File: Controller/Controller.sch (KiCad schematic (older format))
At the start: 33 parts

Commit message: Controller schematic...
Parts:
- removed J?: USB_B_Mini, symbol Connector:USB_B_Mini
- removed U?: ATmega328P-AU, Package_QFP:TQFP-32_7x7mm_P0.8mm, symbol MCU_Microchip_ATmega:ATmega328P-AU
- added C1, C2: 330uF, symbol Device:CP_Small
- added C10, C12: 100nF, Capacitor_SMD:C_0805_2012Metric, symbol Device:C_Small
- added C11: 4u7, symbol Device:CP_Small
- added C21, C22, C24: 100n, Capacitor_SMD:C_0805_2012Metric, symbol Device:C_Small
- added C3, C6: 10nF, Capacitor_SMD:C_0805_2012Metric, symbol Device:C_Small
- added C4, C5: 100uF, symbol Device:CP_Small
- added C9: 10uF, Capacitor_SMD:C_0805_2012Metric, symbol Device:C_Small
- added D1, D2: BLUE, LED_SMD:LED_0805_2012Metric, symbol Device:LED
- added D3: SS1P3L, Diode_SMD:D_SOD-123, symbol Device:D
- added D4: ORANGE, LED_SMD:LED_0805_2012Metric, symbol Device:LED
- added D5: GREEN, LED_SMD:LED_0805_2012Metric, symbol Device:LED
- added D8: RED, LED_SMD:LED_0805_2012Metric, symbol Device:LED
- added F1: 4A, symbol Device:Fuse
- added F2: 1A, symbol Device:Fuse
- added F3: 500mA, Fuse:Fuse_1812_4532Metric, symbol Device:Polyfuse
- added J2: CON_15V, Connector_JST:JST_XH_B2B-XH-A_1x02_P2.50mm_Vertical, symbol Connector_Generic:Conn_01x02
- added J5: CON_5V, Connector_JST:JST_XH_B2B-XH-A_1x02_P2.50mm_Vertical, symbol Connector_Generic:Conn_01x02
- added J6: CON_5V_AUX, Connector_JST:JST_XH_B2B-XH-A_1x02_P2.50mm_Vertical, symbol Connector_Generic:Conn_01x02
- added J7: CON_USB_A, Connector_USB:USB_B_TE_5787834_Vertical, symbol Connector:USB_A
- added L1, L2, L3: 10uH, symbol Device:L_Small
- added Q1, Q2: SI4435FDY, Package_SO:SO-8_5.3x6.2mm_P1.27mm, symbol ak:Q_PMOS_SSSGDDDD
- added Q3: SQ2309ES, Package_TO_SOT_SMD:SOT-23, symbol Device:Q_PMOS_GSD
- added R1, R2, R3, R4, R7: 1k, Resistor_SMD:R_0805_2012Metric, symbol Device:R_Small
- added R11, R12: 10k, Resistor_SMD:R_0805_2012Metric, symbol Device:R_Small
- added R13: 330R, Resistor_SMD:R_0805_2012Metric, symbol Device:R_Small
- added SW1: SW_Push, Button_Switch_THT:SW_PUSH_6mm, symbol Switch:SW_Push
- added TP1, TP10, TP11, TP12, TP13, TP14, TP15, TP16, TP17, TP2, TP3, TP4, TP5, TP6, TP7, TP8, TP9: TestPoint_Alt, symbol Connector:TestPoint_Alt
- added U2: ATmega328P-AU, Package_QFP:TQFP-32_7x7mm_P0.8mm, symbol ak:ATmega328P-AU
- added U4: 74AHC1G14, Package_TO_SOT_SMD:SOT-23-5, symbol ak:74AHC1G14
- added U5: MCP6001-OT, Package_TO_SOT_SMD:SOT-23-5, symbol Amplifier_Operational:MCP6001-OT
- C13, C15, C16, C18, C20, C7, C8: renamed from C?; footprint (none) -> Capacitor_SMD:C_0805_2012Metric
- C14, C17, C19: renamed from C?; value 1uF -> 10nF; footprint (none) -> Capacitor_SMD:C_0805_2012Metric
- C23: renamed from C?; value 100nF -> 10nF; footprint (none) -> Capacitor_SMD:C_0805_2012Metric
- D6: renamed from D?; value RX RED -> RX ORANGE; footprint (none) -> LED_SMD:LED_0805_2012Metric
- D7: renamed from D?; footprint (none) -> LED_SMD:LED_0805_2012Metric
- F4: renamed from F?; footprint (none) -> Fuse:Fuse_1812_4532Metric
- J1: renamed from J?; value Signal out -> CON_TLC
- J3: renamed from J?; value ICSP -> CON_ICSP; footprint (none) -> Connector_IDC:IDC-Header_2x03_P2.54mm_Vertical
- R5, R6, R8, R9: renamed from R?; footprint (none) -> Resistor_SMD:R_0805_2012Metric
- Y1: renamed from Y?; value Resonator_Small -> 16MHz
- gave numbers to parts that had none: 10
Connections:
- net labels added: +15V, +3V3, +5VD, +BATT, FTDI_RX, FTDI_TX, LDR, LED, RTC_1PPS, RTC_32K, RTC_SCL, RTC_SDA, TLC_BLANK, TLC_LAT, TLC_SCL, TLC_SDA, USBD+, USBD-, ~RESET~, ~RTC_RST~
- net labels removed: BLANK, LAT, SCLK, SDAT, VCC, Vdrive
- wire segments 152 -> 306
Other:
- note added: "AUX POWER"
- note added: "DC SUPPLY"
- note added: "ICSP CONNECTOR"
- note added: "KICAD POWER FLAGS"
- note added: "LED DRIVER SIGNAL CONNECTOR"
- note added: "LIGHT SENSOR"
- note added: "MICROCONTROLLER"
- note added: "MOUNTING HOLES"
- note added: "REAL TIME CLOCK"
- note added: "RESET BUTTON"
- note added: "TEST POINTS"
- note added: "USB <-> SERIAL CONVERTER"
- note added: "USB POWER"
- moved on the sheet: C13, C14, C15, C16, C17, C18, C19, C20, C23, C7, C8, D6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

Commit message: Controller...
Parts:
- removed BT1: Battery_Cell, symbol Device:Battery_Cell
- removed C9: 10uF, Capacitor_SMD:C_0805_2012Metric, symbol Device:C_Small
- removed H3, H4: MountingHole_Pad, MountingHole:MountingHole_3.2mm_M3_Pad_Via, symbol Mechanical:MountingHole_Pad
- removed RV1: 100k, symbol Device:R_POT_TRIM
- added C25: 100n, Capacitor_SMD:C_0805_2012Metric, symbol Device:C_Small
- added C26: 1F, ak:FC0H105ZFTBR44, symbol Device:CP
- added C9: 4u7, Capacitor_SMD:C_Elec_4x5.8, symbol Device:CP_Small
- added D9: BAS716, Diode_SMD:D_SOD-523, symbol Device:D_Small
- added R14: 100R, Resistor_SMD:R_0805_2012Metric, symbol Device:R_Small
- added U6: MCP4012-xxxxCH, Package_TO_SOT_SMD:SOT-23-6, symbol Potentiometer_Digital:MCP4012-xxxxCH
- C1, C2: footprint (none) -> Capacitor_SMD:CP_Elec_10x10
- C11: footprint (none) -> Capacitor_SMD:C_Elec_4x5.8
- C4, C5: footprint (none) -> Capacitor_SMD:C_Elec_6.3x5.8
- F1, F2: footprint (none) -> ak:Fuseholder_SMD_Littelfuse_154
- J4: footprint ak:HARWIN_M20-7910842R -> ak:HARWIN_M20-8890845
- L1, L2, L3: footprint (none) -> Inductor_SMD:L_0805_2012Metric
- Q1, Q2: symbol ak:Q_PMOS_SSSGDDDD -> Controller-rescue:Q_PMOS_SSSGDDDD-ak
- TP1, TP10, TP11, TP12, TP13, TP14, TP15, TP16, TP17, TP2, TP3, TP4, TP5, TP6, TP7, TP8, TP9: footprint (none) -> TestPoint:TestPoint_Loop_D2.60mm_Drill1.6mm_Beaded
- U2: symbol ak:ATmega328P-AU -> Controller-rescue:ATmega328P-AU-ak
- Y1: footprint (none) -> ak:CSTNE
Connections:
- net labels added: POT_U~D~, ~POT_CS~
- wire segments 306 -> 321
- no-connect marks 0 -> 17
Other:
- moved on the sheet: C10, C19, C20, C21, C22, C23, C24, D4, F3, H1, H2, J6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

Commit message: Ground vias digit+colon. Placement/routing controller
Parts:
- C14, C15, C16, C17, C18, C19, C20: footprint Capacitor_SMD:C_0805_2012Metric -> Capacitor_SMD:C_0603_1608Metric
- J7: footprint Connector_USB:USB_B_TE_5787834_Vertical -> ak:UJ2-BV-1-TH
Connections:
- wire segments 321 -> 324
- no-connect marks 17 -> 16
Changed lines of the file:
@@
 EESchema Schematic File Version 4
 LIBS:Controller-cache
-EELAYER 29 0
+EELAYER 30 0
 EELAYER END
 $Descr A3 16535 11693
@@
 F 0 "C20" V 3500 6100 50  0000 C CNN
 F 1 "100nF" V 3500 5850 50  0000 C CNN
-F 2 "Capacitor_SMD:C_0805_2012Metric" H 3450 6000 50  0001 C CNN
+F 2 "Capacitor_SMD:C_0603_1608Metric" H 3450 6000 50  0001 C CNN
 F 3 "~" H 3450 6000 50  0001 C CNN
 	1    3450 6000
@@
 F 0 "C19" V 3500 5900 50  0000 C CNN
 F 1 "10nF" V 3500 5650 50  0000 C CNN
-F 2 "Capacitor_SMD:C_0805_2012Metric" H 3450 5800 50  0001 C CNN
+F 2 "Capacitor_SMD:C_0603_1608Metric" H 3450 5800 50  0001 C CNN
 F 3 "~" H 3450 5800 50  0001 C CNN
 	1    3450 5800
@@
 U 1 1 5D9BB567
 P 12850 4850
-F 0 "C18" H 12950 4800 50  0000 R CNN
+F 0 "C18" H 13050 4750 50  0000 R CNN
 F 1 "100nF" H 13100 4950 50  0000 R CNN
-F 2 "Capacitor_SMD:C_0805_2012Metric" H 12850 4850 50  0001 C CNN
+F 2 "Capacitor_SMD:C_0603_1608Metric" H 12850 4850 50  0001 C CNN
 F 3 "~" H 12850 4850 50  0001 C CNN
 	1    12850 4850
@@
 F 0 "C15" V 13200 4650 50  0000 R CNN
 F 1 "100nF" V 13200 5000 50  0000 R CNN
-F 2 "Capacitor_SMD:C_0805_2012Metric" H 13250 4700 50  0001 C CNN
+F 2 "Capacitor_SMD:C_0603_1608Metric" H 13250 4700 50  0001 C CNN
 F 3 "~" H 13250 4700 50  0001 C CNN
 	1    13250 4700
@@
 F 0 "C14" V 13000 4650 50  0000 R CNN
 F 1 "10nF" V 13000 4950 50  0000 R CNN
-F 2 "Capacitor_SMD:C_0805_2012Metric" H 13050 4700 50  0001 C CNN
+F 2 "Capacitor_SMD:C_0603_1608Metric" H 13050 4700 50  0001 C CNN
 F 3 "~" H 13050 4700 50  0001 C CNN
 	1    13050 4700
@@
 F 0 "C17" V 14100 4650 50  0000 R CNN
 F 1 "10nF" V 14100 4950 50  0000 R CNN
-F 2 "Capacitor_SMD:C_0805_2012Metric" H 14050 4700 50  0001 C CNN
+F 2 "Capacitor_SMD:C_0603_1608Metric" H 14050 4700 50  0001 C CNN
 F 3 "~" H 14050 4700 50  0001 C CNN
 	1    14050 4700
@@
 F 0 "C16" V 13900 4650 50  0000 R CNN
 F 1 "100nF" V 13900 5000 50  0000 R CNN
-F 2 "Capacitor_SMD:C_0805_2012Metric" H 13850 4700 50  0001 C CNN
+F 2 "Capacitor_SMD:C_0603_1608Metric" H 13850 4700 50  0001 C CNN
 F 3 "~" H 13850 4700 50  0001 C CNN
 	1    13850 4700
@@
 Text Label 10800 5400 0    50   ~ 10
 TLC_SCL
-Text Label 10800 5000 0    50   ~ 0
+Text Label 10800 5200 0    50   ~ 0
 TLC_LAT
 Text Label 10800 5100 0    50   ~ 0
@@
 F 0 "J7" H 5900 5150 50  0000 C CNN
 F 1 "CON_USB_A" H 6300 4450 50  0000 C CNN
-F 2 "Connector_USB:USB_B_TE_5787834_Vertical" H 6200 4750 50  0001 C CNN
+F 2 "ak:UJ2-BV-1-TH" H 6200 4750 50  0001 C CNN
 F 3 " ~" H 6200 4750 50  0001 C CNN
 	1    6050 4800
@@
 Wire Wire Line
 	2450 2550 2800 2550
-Wire Wire Line
-	11250 4200 10800 4200
-Text Label 10950 4200 2    50   ~ 0
-LED
 Wire Notes Line
 	11750 1150 13000 1150
@@
 	10800 4400 11250 4400
 NoConn ~ 12600 5100
-NoConn ~ 12600 5200
-NoConn ~ 11250 5200
 NoConn ~ 11250 6300
 NoConn ~ 11250 6400
@@
 	-1   0    0    1
 $EndComp
+Wire Wire Line
+	11250 5200 10800 5200
+Wire Wire Line
+	12600 5200 12650 5200
+Wire Wire Line
+	12650 5200 12650 5400
+Wire Wire Line
+	12650 5400 13650 5400
+NoConn ~ 11250 4200
 $EndSCHEMATC

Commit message: Routing controller
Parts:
- removed D9: BAS716, Diode_SMD:D_SOD-523, symbol Device:D_Small
- added D9: SS1P3L, Diode_SMD:D_SOD-123, symbol Device:D
- added R15: 47k, Resistor_SMD:R_0603_1608Metric, symbol Device:R_Small
- C10, C12, C13, C21, C22, C23, C24, C25, C6, C7, C8: footprint Capacitor_SMD:C_0805_2012Metric -> Capacitor_SMD:C_0603_1608Metric
- D1, D2, D4, D5, D6, D7, D8: footprint LED_SMD:LED_0805_2012Metric -> LED_SMD:LED_0603_1608Metric
- R1, R11, R12, R13, R14, R2, R3, R4, R5, R6, R7, R8, R9: footprint Resistor_SMD:R_0805_2012Metric -> Resistor_SMD:R_0603_1608Metric
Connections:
- net labels removed: +3V3
- wire segments 324 -> 323
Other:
- moved on the sheet: C23, R14

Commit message: layout...
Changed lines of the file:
@@
 EESchema Schematic File Version 4
 LIBS:Controller-cache
-EELAYER 29 0
+EELAYER 30 0
 EELAYER END
 $Descr A3 16535 11693
@@
 Wire Notes Line
 	950  9350 950  7500
+Text Label 10800 4300 0    50   ~ 0
+POT_U~D~
 Text Label 10800 4400 0    50   ~ 0
-POT_U~D~
-Text Label 10800 4300 0    50   ~ 0
 ~POT_CS~
 Wire Wire Line
@@
 	2750 8700 2750 8550
 $Comp
-L power:+5V #PWR?
+L power:+5V #PWR0104
 U 1 1 5DC2D6B5
 P 5850 7850
-F 0 "#PWR?" H 5850 7700 50  0001 C CNN
+F 0 "#PWR0104" H 5850 7700 50  0001 C CNN
 F 1 "+5V" H 5865 8023 50  0000 C CNN
 F 2 "" H 5850 7850 50  0001 C CNN
@@
 $EndComp
 $Comp
-L power:+5V #PWR?
+L power:+5V #PWR0105
 U 1 1 5DC2D918
 P 6900 7850
-F 0 "#PWR?" H 6900 7700 50  0001 C CNN
+F 0 "#PWR0105" H 6900 7700 50  0001 C CNN
 F 1 "+5V" H 6915 8023 50  0000 C CNN
 F 2 "" H 6900 7850 50  0001 C CNN

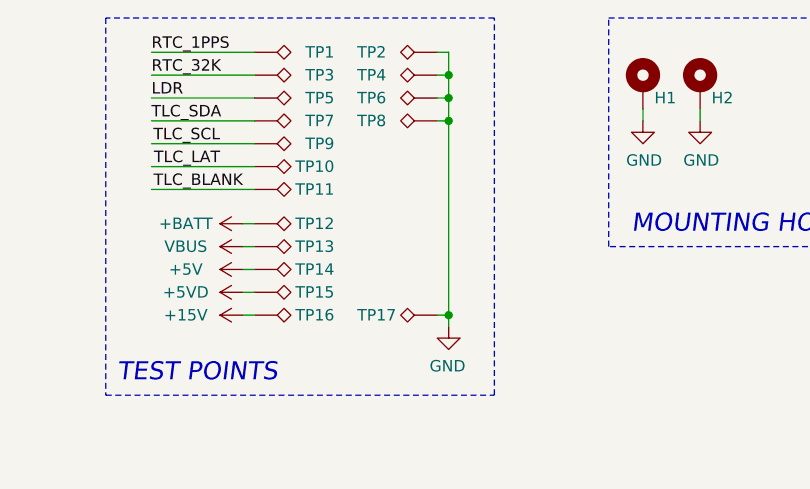
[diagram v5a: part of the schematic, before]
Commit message: Created mounting bracket.
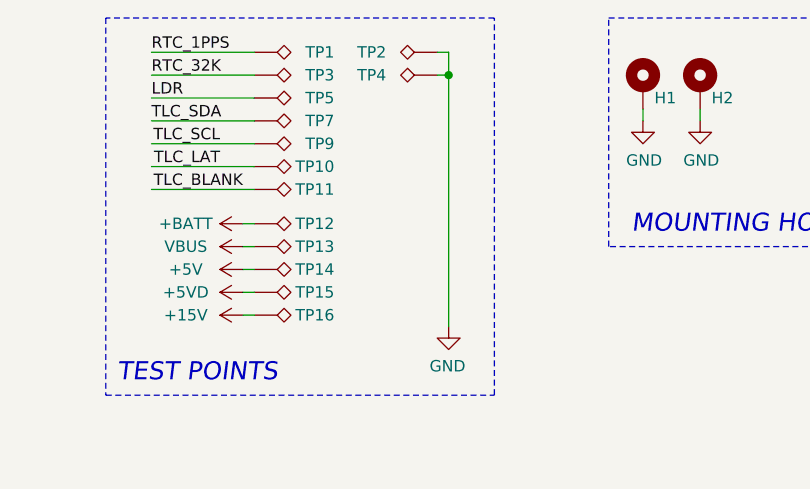
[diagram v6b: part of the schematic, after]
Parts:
- removed TP17, TP4, TP6: TestPoint_Alt, TestPoint:TestPoint_Loop_D2.60mm_Drill1.6mm_Beaded, symbol Connector:TestPoint_Alt
- renumbered TP8 to TP4
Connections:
- wire segments 323 -> 317
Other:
- moved on the sheet: TP4
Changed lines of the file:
@@
 EESchema Schematic File Version 4
-LIBS:Controller-cache
 EELAYER 30 0
 EELAYER END
@@
 	10200 2450 10150 2450
 $Comp
-L Connector:TestPoint_Alt TP8
+L Connector:TestPoint_Alt TP4
 U 1 1 5EAC13B7
-P 11000 1600
-F 0 "TP8" V 11000 1950 50  0000 R CNN
-F 1 "TestPoint_Alt" H 10942 1717 50  0001 R CNN
-F 2 "TestPoint:TestPoint_Loop_D2.60mm_Drill1.6mm_Beaded" H 11200 1600 50  0001 C CNN
-F 3 "~" H 11200 1600 50  0001 C CNN
-	1    11000 1600
+P 11000 1400
+F 0 "TP4" V 11000 1750 50  0000 R CNN
+F 1 "TestPoint_Alt" H 10942 1517 50  0001 R CNN
+F 2 "TestPoint:TestPoint_Loop_D2.60mm_Drill1.6mm_Beaded" H 11200 1400 50  0001 C CNN
+F 3 "~" H 11200 1400 50  0001 C CNN
+	1    11000 1400
 	0    -1   -1   0
 $EndComp
@@
 	10200 1900 9750 1900
 Wire Wire Line
-	11050 1600 11000 1600
-Wire Wire Line
-	11050 1600 11050 2450
-$Comp
-L Connector:TestPoint_Alt TP6
-U 1 1 5EE00DB4
-P 11000 1500
-F 0 "TP6" V 11000 1850 50  0000 R CNN
-F 1 "TestPoint_Alt" H 10942 1617 50  0001 R CNN
-F 2 "TestPoint:TestPoint_Loop_D2.60mm_Drill1.6mm_Beaded" H 11200 1500 50  0001 C CNN
-F 3 "~" H 11200 1500 50  0001 C CNN
-	1    11000 1500
-	0    -1   -1   0
-$EndComp
-Wire Wire Line
-	11050 1500 11000 1500
-Wire Wire Line
-	11050 1500 11050 1600
-Connection ~ 11050 1600
-$Comp
-L Connector:TestPoint_Alt TP4
-U 1 1 5EE33DD9
-P 11000 1400
-F 0 "TP4" V 11000 1750 50  0000 R CNN
-F 1 "TestPoint_Alt" H 10942 1517 50  0001 R CNN
-F 2 "TestPoint:TestPoint_Loop_D2.60mm_Drill1.6mm_Beaded" H 11200 1400 50  0001 C CNN
-F 3 "~" H 11200 1400 50  0001 C CNN
-	1    11000 1400
-	0    -1   -1   0
-$EndComp
-Wire Wire Line
 	11050 1400 11000 1400
-Wire Wire Line
-	11050 1400 11050 1500
+Connection ~ 11050 1400
 $Comp
 L Connector:TestPoint_Alt TP2
@@
 Wire Wire Line
 	11050 1300 11000 1300
-Wire Wire Line
-	11050 1300 11050 1400
-Connection ~ 11050 1500
-Connection ~ 11050 1400
-$Comp
-L Connector:TestPoint_Alt TP17
-U 1 1 5EF945D2
-P 11000 2450
-F 0 "TP17" V 11000 2800 50  0000 R CNN
-F 1 "TestPoint_Alt" H 10942 2567 50  0001 R CNN
-F 2 "TestPoint:TestPoint_Loop_D2.60mm_Drill1.6mm_Beaded" H 11200 2450 50  0001 C CNN
-F 3 "~" H 11200 2450 50  0001 C CNN
-	1    11000 2450
-	0    -1   -1   0
-$EndComp
-Wire Wire Line
-	11000 2450 11050 2450
-Connection ~ 11050 2450
-Wire Wire Line
-	11050 2450 11050 2500
 Wire Notes Line
 	9550 2800 11250 2800
@@
 	-1   0    0    -1
 $EndComp
+Wire Wire Line
+	11050 1400 11050 2500
+Wire Wire Line
+	11050 1300 11050 1400
 $EndSCHEMATC

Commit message: Moved mounting holes. Moved stuff around on controller PCB.
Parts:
- F3, F4: footprint Fuse:Fuse_1812_4532Metric -> ak:Fuse_1812_4532Metric
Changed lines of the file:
@@
 EESchema Schematic File Version 4
+LIBS:Controller-cache
 EELAYER 30 0
 EELAYER END
@@
 F 0 "F4" V 6700 4450 50  0000 C CNN
 F 1 "MF-MSMF050-2 500mA" V 6500 4250 50  0000 C CNN
-F 2 "Fuse:Fuse_1812_4532Metric" H 6650 4250 50  0001 L CNN
+F 2 "ak:Fuse_1812_4532Metric" H 6650 4250 50  0001 L CNN
 F 3 "~" H 6600 4450 50  0001 C CNN
 	1    6600 4450
@@
 F 0 "F3" V 1750 4050 50  0000 C CNN
 F 1 "500mA" V 1550 4050 50  0000 C CNN
-F 2 "Fuse:Fuse_1812_4532Metric" H 1700 3850 50  0001 L CNN
+F 2 "ak:Fuse_1812_4532Metric" H 1700 3850 50  0001 L CNN
 F 3 "~" H 1650 4050 50  0001 C CNN
 	1    1650 4050

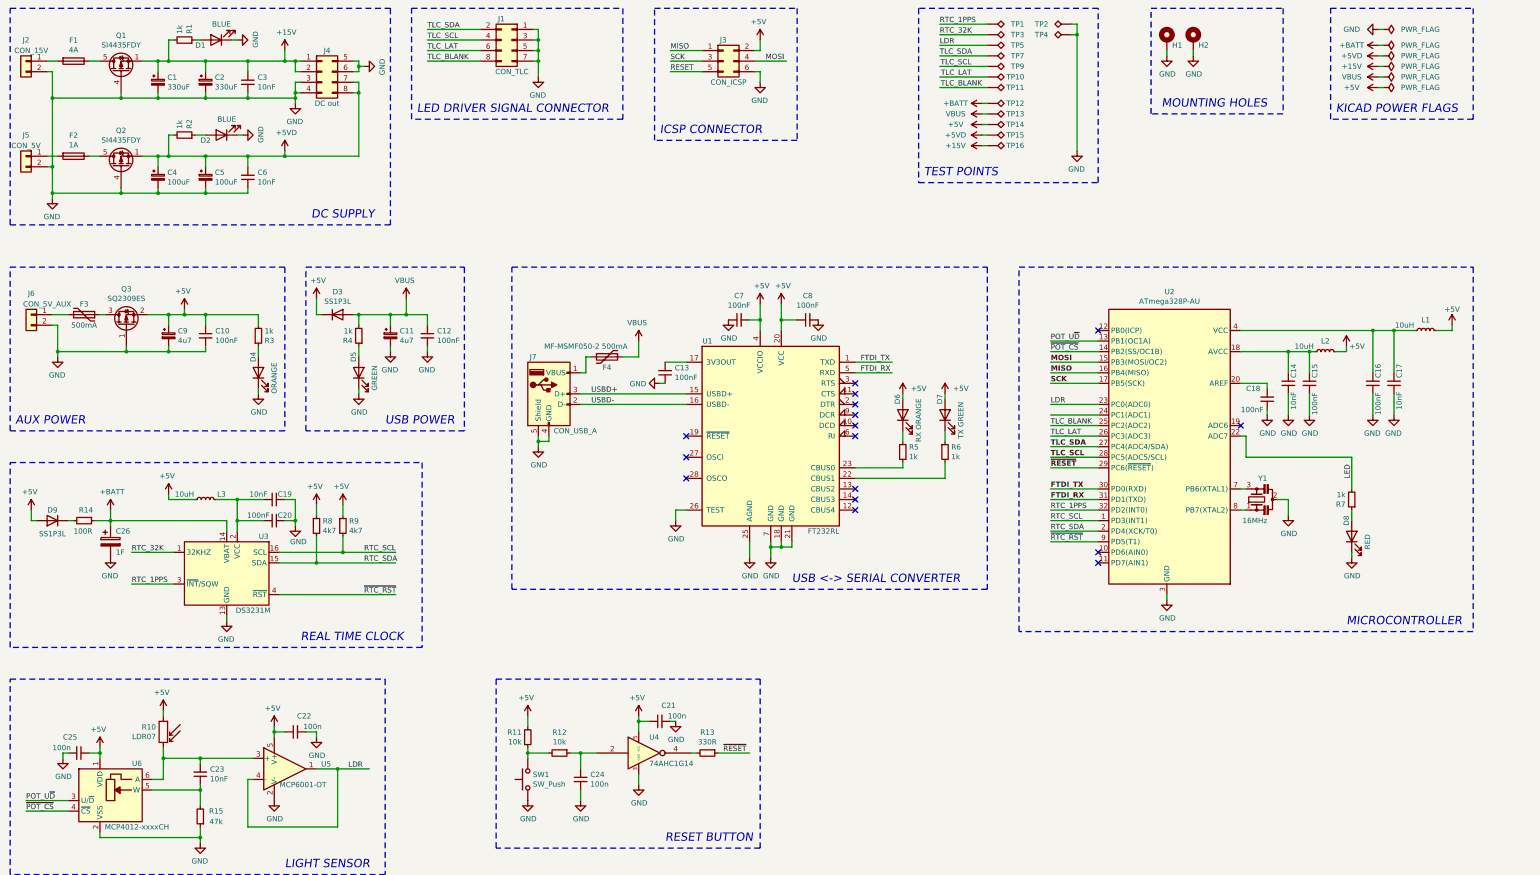
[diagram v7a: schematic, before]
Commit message: Bug fixes: * Reset circuit   - netlabel RESET -> /RESET   - Reset button pulls high   - FTDI DTR connected to reset line * Added pull-ups to RTC outputs * Moved status LED to PC1 TODO: * Add thermal reliefs to copper planes
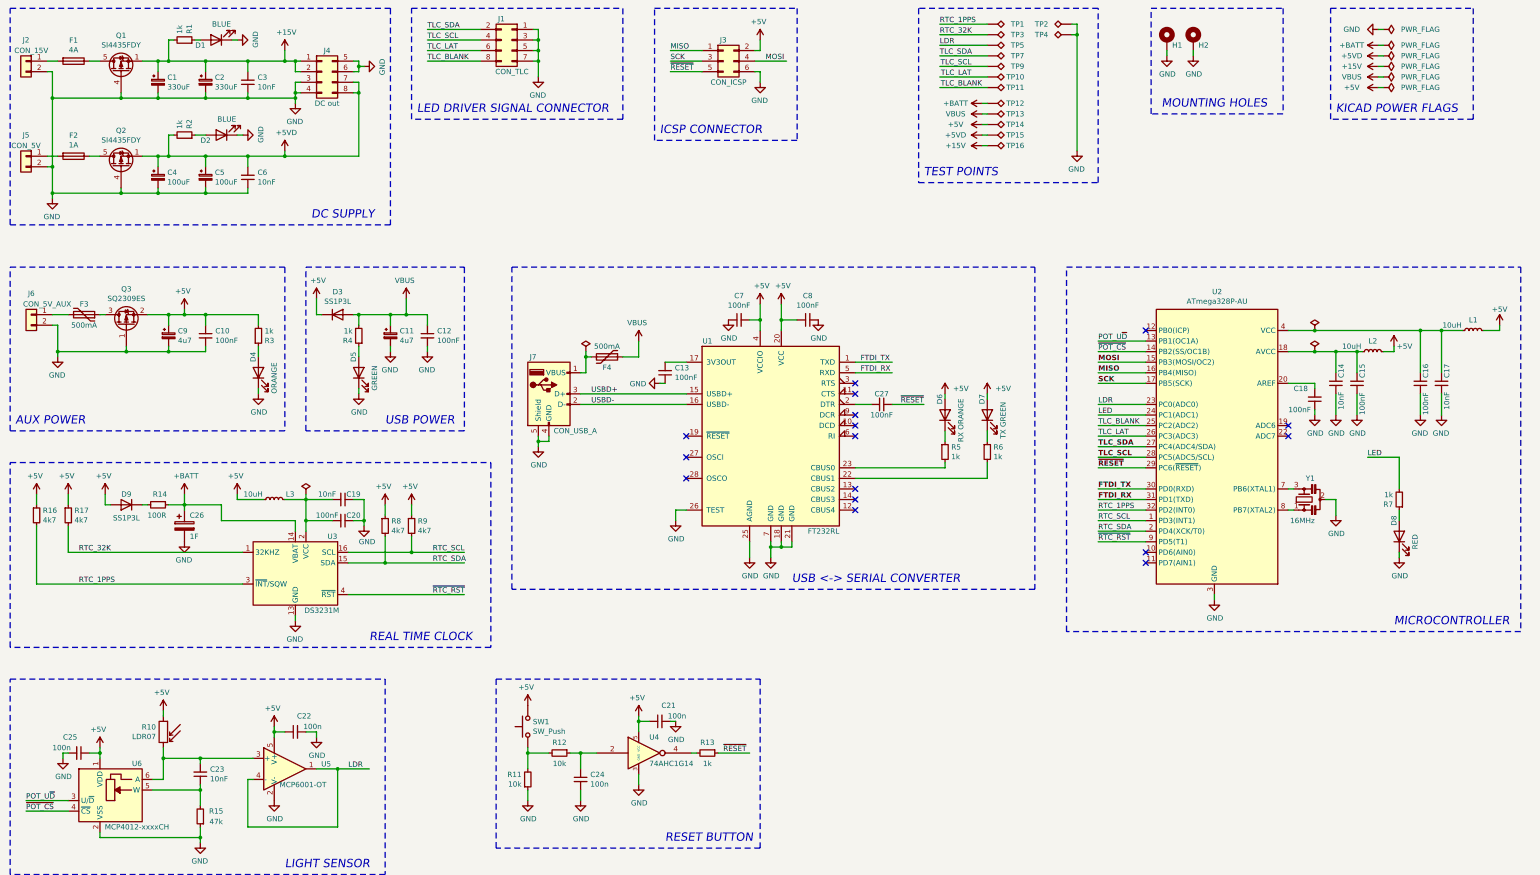
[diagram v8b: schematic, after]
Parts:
- added C27: 100nF, Capacitor_SMD:C_0603_1608Metric, symbol Device:C_Small
- added R16, R17: 4k7, Resistor_SMD:R_0603_1608Metric, symbol Device:R_Small
- F4: value MF-MSMF050-2 500mA -> 500mA
- R13: value 330R -> 1k
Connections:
- net labels removed: RESET
- wire segments 317 -> 327
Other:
- moved on the sheet: C14, C15, C16, C17, C18, C19, C20, C26, D6, D7, D8, D9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
